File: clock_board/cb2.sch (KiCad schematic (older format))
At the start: 39 parts, among them IC1 ATMEGA328-P, P1 POWER, P2 PROGRAMMER, P3 BATT_CONN, P4 LEDB_POWER, P5 LCD_CLK_CONN, P6 DIGIT_POWER, Q1 DGT1, Q2 DGT2, Q3 DGT3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

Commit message: Read the time one 1-second intervals as dictated by the DS3231 square wave.
Fixed a bug in RTC I2C communications where all read bytes were being BCD
decoded.
Got rid of the unused LED pin.
Enabled the 1Hz square wave on the DS3231.
Changed the schematic to no longer use the 32KHz wave and instead connect the
1Hz square wave to INT1, and only trigger INT1 on falling edges.
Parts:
- C7: footprint Capacitors_Elko_ThroughHole:Elko_vert_20x10mm_RM2.5 -> Capacitors_Elko_ThroughHole:Elko_vert_11.2x6.3mm_RM2.5
- P3: footprint Connect:PINHEAD1-2 -> Pin_Headers:Pin_Header_Straight_1x02
- R3, R4: footprint Resistors_ThroughHole:Resistor_Horizontal_RM10mm -> Resistors_ThroughHole:Resistor_Horizontal_RM15mm
- U2: footprint SMD_Packages:SO-16-N -> Housings_SOIC:SOIC-16_7.5x10.3mm_Pitch1.27mm
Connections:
- net at IC1.5 ((PCINT19/OC2B/INT1)PD3): now also U2.3 (~INT~/SQW); no longer SW1.2
- net at IC1.6 ((PCINT20/XCK/T0)PD4): no longer U2.1 (32kHz)
- no-connect marks 12 -> 11
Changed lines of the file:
@@
 F 0 "U2" H 5575 5100 60  0000 C CNN
 F 1 "DS3231" H 5575 5550 60  0000 C CNN
-F 2 "SMD_Packages:SO-16-N" H 5625 5400 60  0001 C CNN
+F 2 "Housings_SOIC:SOIC-16_7.5x10.3mm_Pitch1.27mm" H 5625 5400 60  0001 C CNN
 F 3 "" H 5625 5400 60  0000 C CNN
 	1    5575 5550
@@
 Text GLabel 4850 3375 2    60   Input ~ 0
 I2C_DATA
-NoConn ~ 4925 5400
 $Comp
 L C C2
@@
 F 0 "P3" H 7300 6000 50  0000 C CNN
 F 1 "BATT_CONN" V 7400 5850 50  0000 C CNN
-F 2 "Connect:PINHEAD1-2" H 7300 5850 60  0001 C CNN
+F 2 "Pin_Headers:Pin_Header_Straight_1x02" H 7300 5850 60  0001 C CNN
 F 3 "" H 7300 5850 60  0000 C CNN
 	1    7300 5850
@@
 F 0 "R4" V 5155 3075 50  0000 C CNN
 F 1 "4.7k" V 5075 3075 50  0000 C CNN
-F 2 "Resistors_ThroughHole:Resistor_Horizontal_RM10mm" V 5005 3075 30  0001 C CNN
+F 2 "Resistors_ThroughHole:Resistor_Horizontal_RM15mm" V 5005 3075 30  0001 C CNN
 F 3 "" H 5075 3075 30  0000 C CNN
 	1    5075 3075
@@
 F 0 "R3" V 5155 2925 50  0000 C CNN
 F 1 "4.7k" V 5075 2925 50  0000 C CNN
-F 2 "Resistors_ThroughHole:Resistor_Horizontal_RM10mm" V 5005 2925 30  0001 C CNN
+F 2 "Resistors_ThroughHole:Resistor_Horizontal_RM15mm" V 5005 2925 30  0001 C CNN
 F 3 "" H 5075 2925 30  0000 C CNN
 	1    5075 2925
@@
 F 0 "C7" H 9675 1025 50  0000 L CNN
 F 1 "10uF" H 9350 925 50  0000 L CNN
-F 2 "Capacitors_Elko_ThroughHole:Elko_vert_20x10mm_RM2.5" H 9688 775 30  0001 C CNN
+F 2 "Capacitors_Elko_ThroughHole:Elko_vert_11.2x6.3mm_RM2.5" H 9688 775 30  0001 C CNN
 F 3 "" H 9650 925 60  0000 C CNN
 	1    9650 925
@@
 	5275 3075 5225 3075
 Connection ~ 5275 2925
-Wire Wire Line
-	3000 4325 3425 4325
-Wire Wire Line
-	3425 4325 3425 5200
-Wire Wire Line
-	3425 5200 4925 5200
-Wire Wire Line
-	3000 4225 3050 4225
-Wire Wire Line
-	3050 4225 3050 5625
 Wire Wire Line
 	3000 4425 3100 4425
@@
 Wire Wire Line
 	4550 6225 7100 6225
+Wire Wire Line
+	3000 4225 3050 4225
+Wire Wire Line
+	3050 4225 3050 4250
+Wire Wire Line
+	3050 4250 3675 4250
+Wire Wire Line
+	3675 4250 3675 4475
+Wire Wire Line
+	3675 4475 4825 4475
+Wire Wire Line
+	4825 4475 4825 5400
+Wire Wire Line
+	4825 5400 4925 5400
 $EndSCHEMATC

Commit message: Add the pullup resistor for the DS3231 square wave.
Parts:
- added R?: 10k, symbol R
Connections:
- net VCC: now also R?.2
- net at IC1.5 ((PCINT19/OC2B/INT1)PD3), U2.3 (~INT~/SQW): now also R?.1
- net at IC1.6 ((PCINT20/XCK/T0)PD4): now also SW1.2
- no-connect marks 11 -> 12
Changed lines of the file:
@@
 	3675 4250 3675 4475
 Wire Wire Line
-	3675 4475 4825 4475
+	3925 5400 4925 5400
 Wire Wire Line
-	4825 4475 4825 5400
+	3050 5625 3050 4325
 Wire Wire Line
-	4825 5400 4925 5400
+	3050 4325 3000 4325
+$Comp
+L R R?
+U 1 1 5635938B
+P 4150 4900
+F 0 "R?" V 4230 4900 50  0000 C CNN
+F 1 "10k" V 4150 4900 50  0000 C CNN
+F 2 "" V 4080 4900 30  0000 C CNN
+F 3 "" H 4150 4900 30  0000 C CNN
+	1    4150 4900
+	-1   0    0    1
+$EndComp
+$Comp
+L VCC #PWR?
+U 1 1 56359432
+P 4150 4650
+F 0 "#PWR?" H 4150 4500 50  0001 C CNN
+F 1 "VCC" H 4150 4800 50  0000 C CNN
+F 2 "" H 4150 4650 60  0000 C CNN
+F 3 "" H 4150 4650 60  0000 C CNN
+	1    4150 4650
+	1    0    0    -1
+$EndComp
+Wire Wire Line
+	4150 5400 4150 5050
+Wire Wire Line
+	4150 4750 4150 4650
+Wire Wire Line
+	3925 5400 3925 4475
+Wire Wire Line
+	3925 4475 3675 4475
+Connection ~ 4150 5400
+NoConn ~ 4925 5200
 $EndSCHEMATC

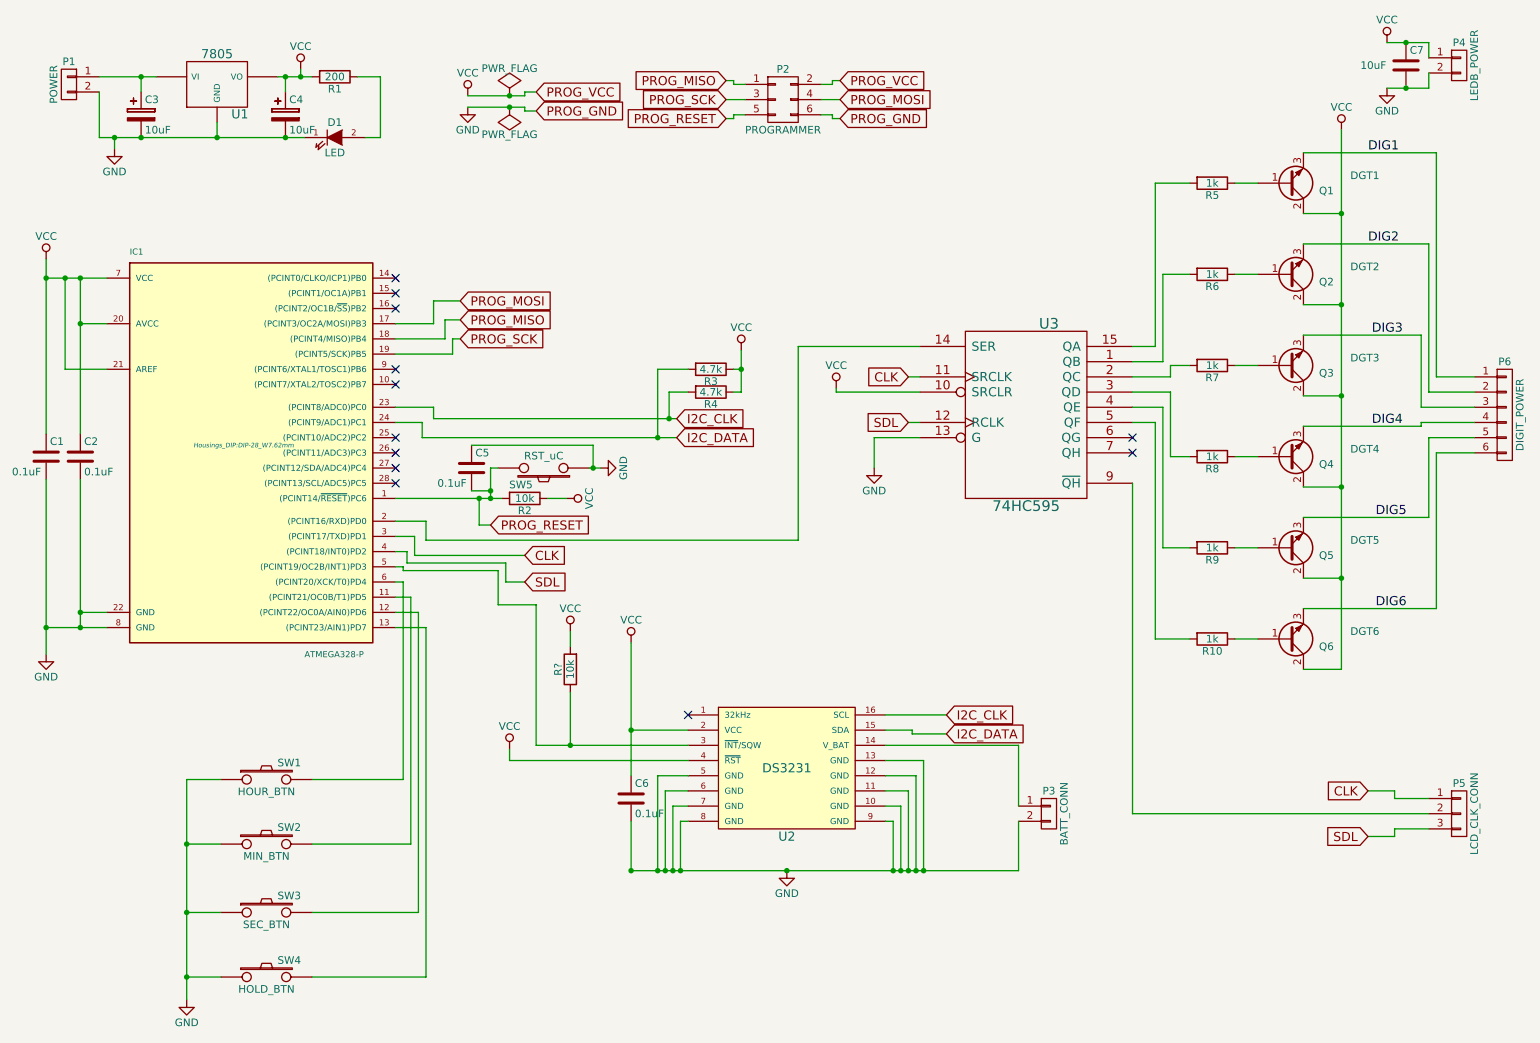
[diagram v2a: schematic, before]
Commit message: Clock board Rev A with routing and placement.
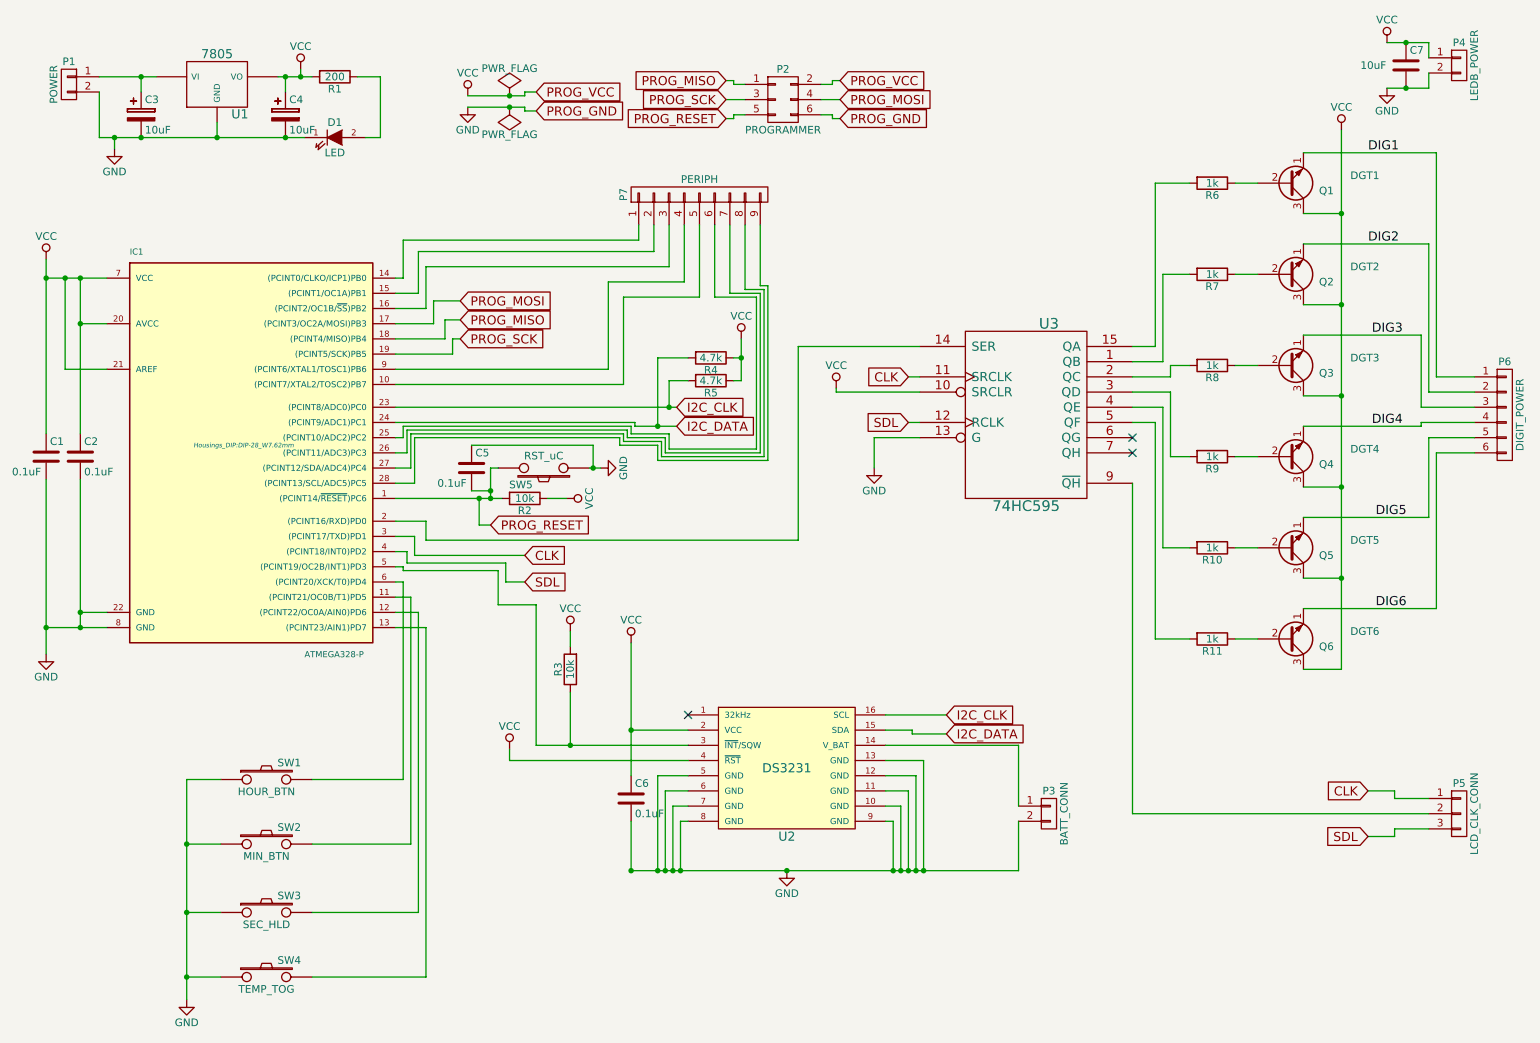
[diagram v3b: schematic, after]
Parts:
- removed Q1: DGT1, Housings_TO-92:TO-92_Inline_Narrow_Oval, symbol Q_NPN_BCE
- removed Q2: DGT2, Housings_TO-92:TO-92_Inline_Narrow_Oval, symbol Q_NPN_BCE
- removed Q3: DGT3, Housings_TO-92:TO-92_Inline_Narrow_Oval, symbol Q_NPN_BCE
- removed Q4: DGT4, Housings_TO-92:TO-92_Inline_Narrow_Oval, symbol Q_NPN_BCE
- removed Q5: DGT5, Housings_TO-92:TO-92_Inline_Narrow_Oval, symbol Q_NPN_BCE
- removed Q6: DGT6, Housings_TO-92:TO-92_Inline_Narrow_Oval, symbol Q_NPN_BCE
- added P7: PERIPH, Pin_Headers:Pin_Header_Straight_1x09, symbol CONN_01X09
- added Q1: DGT1, Housings_TO-92:TO-92_Inline_Narrow_Oval, symbol Q_NPN_EBC
- added Q2: DGT2, Housings_TO-92:TO-92_Inline_Narrow_Oval, symbol Q_NPN_EBC
- added Q3: DGT3, Housings_TO-92:TO-92_Inline_Narrow_Oval, symbol Q_NPN_EBC
- added Q4: DGT4, Housings_TO-92:TO-92_Inline_Narrow_Oval, symbol Q_NPN_EBC
- added Q5: DGT5, Housings_TO-92:TO-92_Inline_Narrow_Oval, symbol Q_NPN_EBC
- added Q6: DGT6, Housings_TO-92:TO-92_Inline_Narrow_Oval, symbol Q_NPN_EBC
- R3: renamed from R?; footprint (none) -> Resistors_ThroughHole:Resistor_Horizontal_RM10mm
- R4: renamed from R3; footprint Resistors_ThroughHole:Resistor_Horizontal_RM15mm -> Resistors_ThroughHole:Resistor_Horizontal_RM10mm
- R5: renamed from R4; footprint Resistors_ThroughHole:Resistor_Horizontal_RM15mm -> Resistors_ThroughHole:Resistor_Horizontal_RM10mm
- SW3: value SEC_BTN -> SEC_HLD
- SW4: value HOLD_BTN -> TEMP_TOG
- renumbered R9 to R10, R10 to R11, R5 to R6, R6 to R7, R7 to R8, R8 to R9
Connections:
- net DIG1: now also Q1.1 (E)
- net DIG2: now also Q2.1 (E)
- net DIG3: now also Q3.1 (E)
- net DIG4: now also Q4.1 (E)
- net DIG5: now also Q5.1 (E)
- net DIG6: now also Q6.1 (E)
- net VCC: now also Q1.3 (C), Q2.3 (C), Q3.3 (C), Q4.3 (C), Q5.3 (C), Q6.3 (C)
- net at IC1.10 ((PCINT7/XTAL2/TOSC2)PB7): now also P7.5 (P5)
- net at IC1.14 ((PCINT0/CLKO/ICP1)PB0): now also P7.1 (P1)
- net at IC1.15 ((PCINT1/OC1A)PB1): now also P7.2 (P2)
- net at IC1.16 ((PCINT2/OC1B/~SS~)PB2): now also P7.3 (P3)
- net at IC1.25 ((PCINT10/ADC2)PC2): now also P7.6 (P6)
- net at IC1.26 ((PCINT11/ADC3)PC3): now also P7.7 (P7)
- net at IC1.27 ((PCINT12/SDA/ADC4)PC4): now also P7.8 (P8)
- net at IC1.28 ((PCINT13/SCL/ADC5)PC5): now also P7.9 (P9)
- net at IC1.9 ((PCINT6/XTAL1/TOSC1)PB6): now also P7.4 (P4)
- net at R7.1: now also Q2.2 (B)
- net at R8.1: now also Q3.2 (B)
- net at R9.1: now also Q4.2 (B)
- net at R10.1: now also Q5.2 (B)
- net at R6.1: now also Q1.2 (B)
- net at R11.1: now also Q6.2 (B)
- no-connect marks 12 -> 3
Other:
- moved on the sheet: R4, R5
